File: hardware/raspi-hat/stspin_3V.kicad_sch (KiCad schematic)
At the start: 4 parts

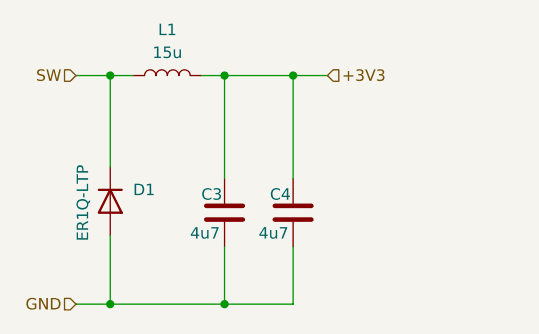
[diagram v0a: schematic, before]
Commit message: added more parts
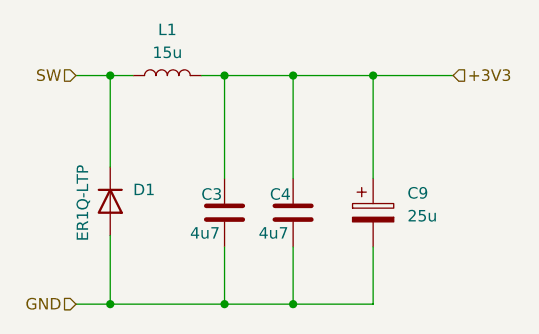
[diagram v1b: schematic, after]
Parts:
- added C9: 25u, Capacitor_SMD:CP_Elec_5x5.3, symbol Device:C_Polarized
- L1: footprint (none) -> Inductor_SMD:L_1008_2520Metric
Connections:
- net +3V3: now also C9.1
- net GND: now also C9.2
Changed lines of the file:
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@@
+	)
+	(junction
+		(at 146.05 102.87)
+		(diameter 0)
+		(color 0 0 0 0)
 	)
 	(junction
@@
 	)
 	(junction
+		(at 154.94 77.47)
+		(diameter 0)
+		(color 0 0 0 0)
+	)
+	(junction
 		(at 138.43 77.47)
 		(diameter 0)
@@
 	(wire
 		(pts
+			(xy 154.94 102.87) (xy 146.05 102.87)
+		)
+		(stroke
+			(width 0)
+			(type default)
+		)
+	)
+	(wire
+		(pts
 			(xy 138.43 102.87) (xy 146.05 102.87)
 		)
@@
 	(wire
 		(pts
-			(xy 146.05 77.47) (xy 149.86 77.47)
+			(xy 146.05 77.47) (xy 154.94 77.47)
 		)
 		(stroke
@@
 	(wire
 		(pts
+			(xy 154.94 96.52) (xy 154.94 102.87)
+		)
+		(stroke
+			(width 0)
+			(type default)
+		)
+	)
+	(wire
+		(pts
 			(xy 125.73 77.47) (xy 128.27 77.47)
 		)
@@
 	(wire
 		(pts
+			(xy 154.94 77.47) (xy 154.94 88.9)
+		)
+		(stroke
+			(width 0)
+			(type default)
+		)
+	)
+	(wire
+		(pts
 			(xy 121.92 102.87) (xy 125.73 102.87)
 		)
@@
 		(pts
 			(xy 138.43 102.87) (xy 138.43 96.52)
+		)
+		(stroke
+			(width 0)
+			(type default)
+		)
+	)
+	(wire
+		(pts
+			(xy 154.94 77.47) (xy 163.83 77.47)
 		)
 		(stroke
@@
 	(hierarchical_label "+3V3"
 		(shape input)
-		(at 149.86 77.47 0)
+		(at 163.83 77.47 0)
 		(effects
 			(font
@@
 			)
 		)
-		(property "Footprint" ""
+		(property "Footprint" "Inductor_SMD:L_1008_2520Metric"
 			(at 132.08 77.47 0)
 			(effects
@@
 					(unit 1)
 				)
+			)
+		)
+	)
+	(symbol
+		(lib_id "Device:C_Polarized")
+		(at 154.94 92.71 0)
+		(unit 1)
+		(exclude_from_sim no)
+		(in_bom yes)
+		(on_board yes)
+		(dnp no)
+		(fields_autoplaced yes)
+		(property "Reference" "C9"
+			(at 158.75 90.5509 0)
+			(effects
+				(font
+					(size 1.27 1.27)
+				)
+				(justify left)
+			)
+		)
+		(property "Value" "25u"
+			(at 158.75 93.0909 0)
+			(effects
+				(font
+					(size 1.27 1.27)
+				)
+				(justify left)
+			)
+		)
+		(property "Footprint" "Capacitor_SMD:CP_Elec_5x5.3"
+			(at 155.9052 96.52 0)
+			(effects
+				(font
+					(size 1.27 1.27)
+				)
+				(hide yes)
+			)
+		)
+		(property "Datasheet" "~"
+			(at 154.94 92.71 0)
+			(effects
+				(font
+					(size 1.27 1.27)
+				)
+				(hide yes)
+			)
+		)
+		(property "Description" "Polarized capacitor"
+			(at 154.94 92.71 0)
+			(effects
+				(font
+					(size 1.27 1.27)
+				)
+				(hide yes)
+			)
+		)
+		(pin "1"
+		)
+		(pin "2"
+		)
+		(instances
+			(project ""
+				(path "/4679b2fb-3ee1-4560-bf60-3ee085e43370/deaad7a1-43b1-44a5-8acb-c2303f4b40ea/13758783-7db5-4f77-9a60-4d6a726bc344"
+					(reference "C9")
+					(unit 1)
+				)

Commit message: adapted some parts
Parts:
- L1: footprint Inductor_SMD:L_1008_2520Metric -> Inductor_SMD:L_0603_1608Metric
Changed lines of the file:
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@@
 			)
 		)
-		(property "Footprint" "Inductor_SMD:L_1008_2520Metric"
+		(property "Footprint" "Inductor_SMD:L_0603_1608Metric"
 			(at 132.08 77.47 0)
 			(effects

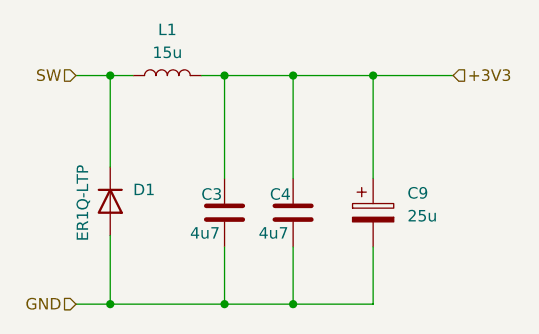
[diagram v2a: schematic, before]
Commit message: - added some more parts for temperature measurement - added capacitor
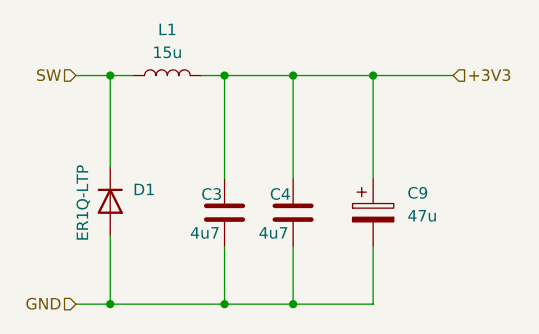
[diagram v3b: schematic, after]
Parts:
- C9: value 25u -> 47u
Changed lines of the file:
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@@
 			)
 		)
-		(property "Value" "25u"
+		(property "Value" "47u"
 			(at 158.75 93.0909 0)
 			(effects
